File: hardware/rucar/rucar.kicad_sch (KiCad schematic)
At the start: 25 parts

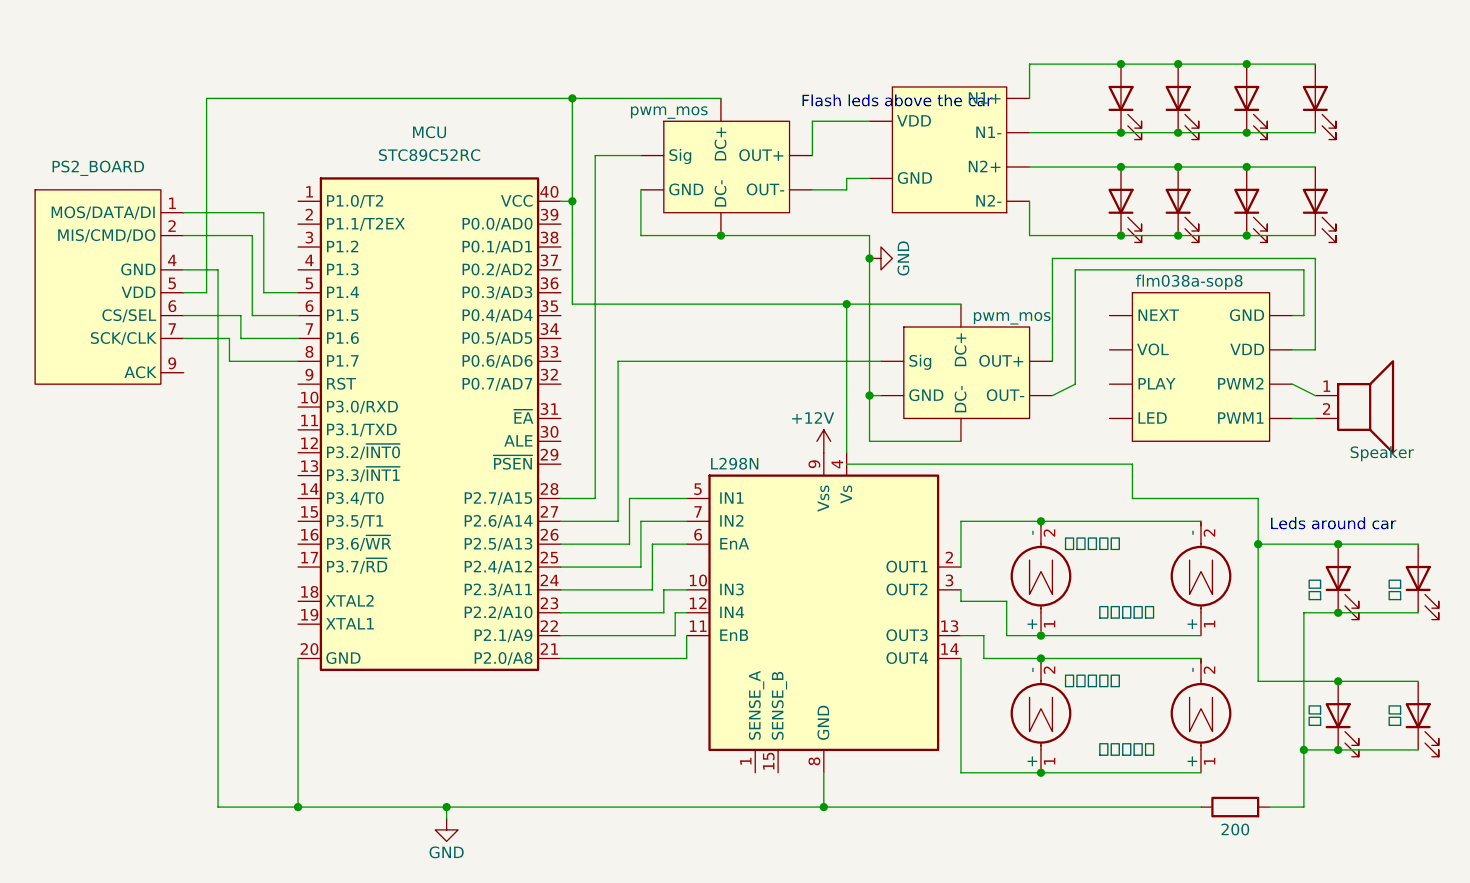
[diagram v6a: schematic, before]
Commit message: change music board to isd1820
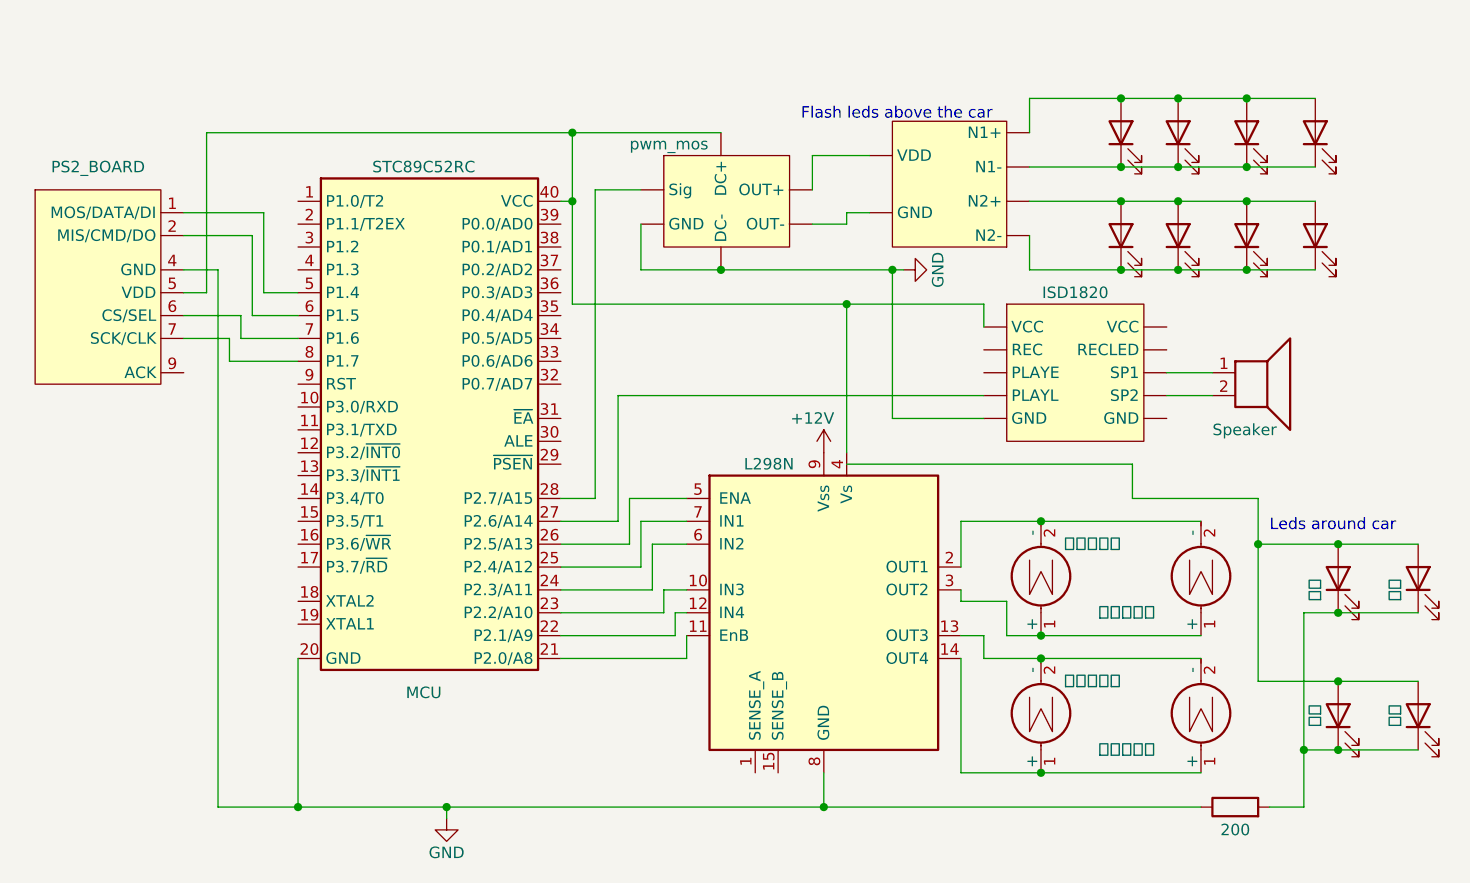
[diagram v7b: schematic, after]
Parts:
- removed U?: L298N, Package_TO_SOT_THT:TO-220-15_P2.54x2.54mm_StaggerOdd_Lead4.58mm_Vertical, symbol Driver_Motor:L298N
- removed U?: pwm_mos, symbol Power_Management:pwm_mos
- removed U?: flm038a-sop8, symbol Audio:flm038a-sop8
- added U?: L298N, Package_TO_SOT_THT:TO-220-15_P2.54x2.54mm_StaggerOdd_Lead4.58mm_Vertical, symbol Driver_Motor:L298N
- added U?: ISD1820, symbol Audio:ISD1820
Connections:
- net +12V: now also U?.9 (Vss)
- net GND: now also U?. (VCC), U?.8 (GND)
- net at MCU.21 (P2.0/A8): now also U?.11 (EnB)
- net at MCU.22 (P2.1/A9): now also U?.12 (IN4)
- net at MCU.23 (P2.2/A10): now also U?.10 (IN3)
- net at MCU.24 (P2.3/A11): now also U?.6 (IN2)
- net at MCU.25 (P2.4/A12): now also U?.7 (IN1)
- net at MCU.26 (P2.5/A13): now also U?.5 (ENA)
- net at MCU.27 (P2.6/A14): now also U?. (VCC)
- net at MCU.40 (VCC), U?. (Sig), U?.5 (VDD): now also U?. (VCC), U?.4 (Vs)
- net at M?.2 (-), M?.2 (-): now also U?.13 (OUT3)
- net at M?.1 (+), M?.1 (+): now also U?.14 (OUT4)
- net at M?.2 (-), M?.2 (-): now also U?.2 (OUT1)
- net at M?.1 (+), M?.1 (+): now also U?.3 (OUT2)
- net at U?. (VDD): now also D?.2 (A), D?.2 (A), D?.2 (A), D?.2 (A); no longer U?. (Sig)
- net at LS?.1: now also U?. (VCC)
- net at LS?.2: now also U?. (VCC)
- new net: U?. (Sig), U?. (VDD) (x2)

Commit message: add AD828
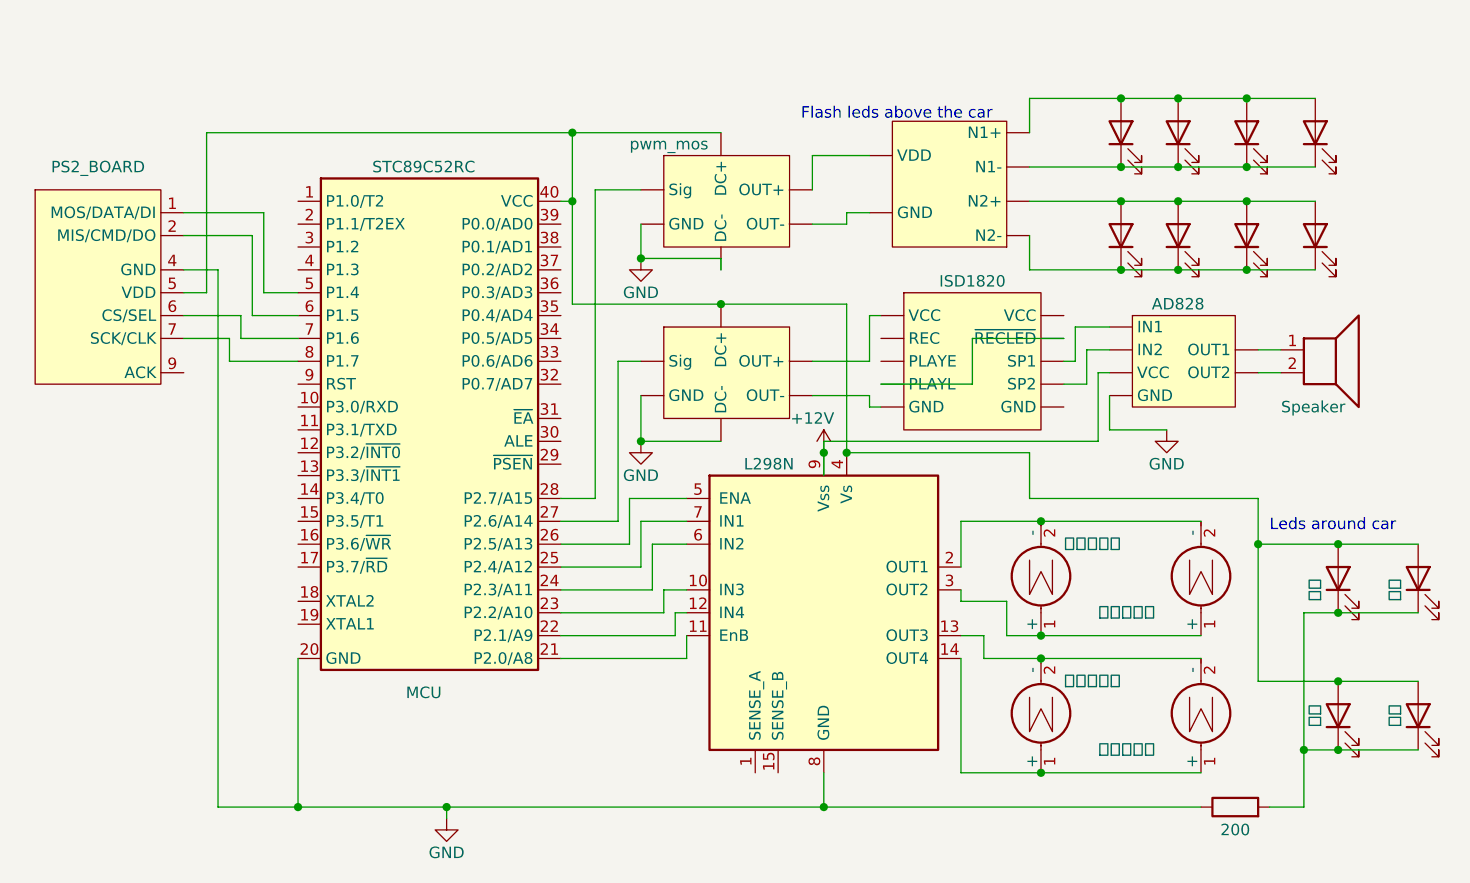
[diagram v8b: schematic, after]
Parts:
- removed U?: ISD1820, symbol Audio:ISD1820
- added U?: pwm_mos, symbol Power_Management:pwm_mos
- added U?: ISD1820, symbol Audio:ISD1820
- added U?: AD828, symbol Audio:AD828
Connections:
- net +12V: now also U?. (VCC)
- net GND: now also U?. (Sig), U?. (VCC)
- net at MCU.27 (P2.6/A14): now also U?. (Sig)
- net at MCU.40 (VCC), U?. (Sig), U?.4 (Vs)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: now also D.2 (A), D.2 (A), D.2 (A), D.2 (A), U?. (Sig)
- net at U?. (VDD): now also D?.2 (A), D?.2 (A), D?.2 (A), D?.2 (A); no longer U?. (Sig)
- net at LS?.1: now also U?. (VCC)
- net at LS?.2: now also U?. (VCC)
- new net: U?. (Sig), U?. (VDD) (x2)
- new net: U?. (Sig), U?. (~{RECLED}) (x2)
- new net: U?. (VCC), U?. (~{RECLED}) (x2)
